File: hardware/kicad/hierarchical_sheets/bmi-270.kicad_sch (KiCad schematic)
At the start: 4 parts

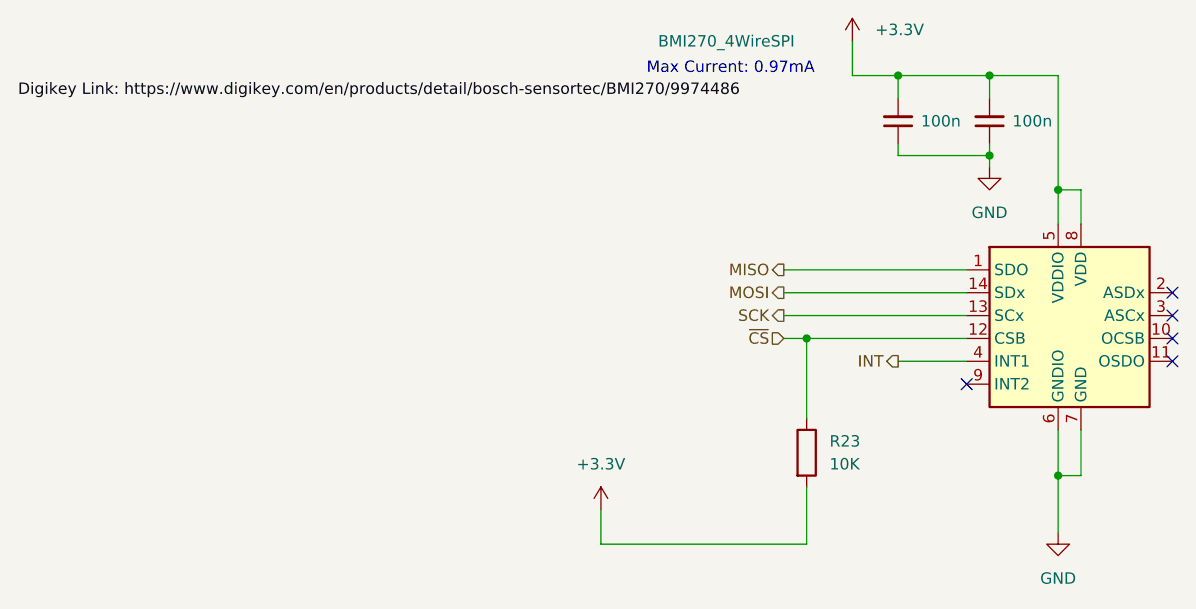
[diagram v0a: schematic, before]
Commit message: assigned footprints
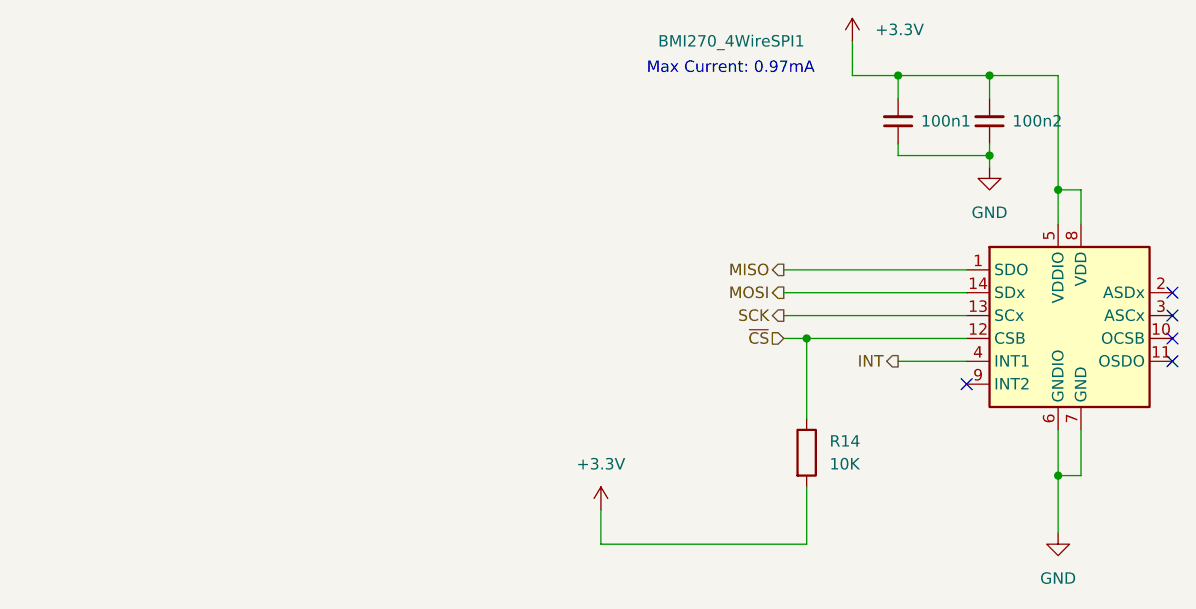
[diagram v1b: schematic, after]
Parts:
- 100n1, 100n2: renamed from 100n; footprint (none) -> Resistor_SMD:R_0603_1608Metric
- R14: renamed from R23; footprint (none) -> Resistor_SMD:R_0603_1608Metric
- renumbered BMI270_4WireSPI to BMI270_4WireSPI1
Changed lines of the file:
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@@
     (effects (font (size 1.27 1.27)) (justify left bottom))
   )
-  (label "Digikey Link: https:{slash}{slash}www.digikey.com{slash}en{slash}products{slash}detail{slash}bosch-sensortec{slash}BMI270{slash}9974486"
-    (at 13.97 77.47 0) (fields_autoplaced)
-    (effects (font (size 1.27 1.27)) (justify left bottom))
-  )
   (hierarchical_label "INT" (shape output) (at 111.76 106.68 180) (fields_autoplaced)
     (effects (font (size 1.27 1.27)) (justify right))
@@
   (symbol (lib_name "C_Small_1") (lib_id "Device:C_Small") (at 111.76 80.01 180) (unit 1)
     (in_bom yes) (on_board yes) (dnp no) (fields_autoplaced)
-    (property "Reference" "100n" (at 114.3 80.0036 0)
+    (property "Reference" "100n1" (at 114.3 80.0036 0)
       (effects (font (size 1.27 1.27)) (justify right))
     )
@@
       (effects (font (size 1.27 1.27)) (justify left) hide)
     )
-    (property "Footprint" "" (at 111.76 80.01 0)
+    (property "Footprint" "Resistor_SMD:R_0603_1608Metric" (at 111.76 80.01 0)
       (effects (font (size 1.27 1.27)) hide)
     )
@@
       (project "FC"
         (path "/54cce219-8b98-4e71-96c4-f9ee784aa3bc/7e43dc21-d4ed-4dfe-b96f-060fb7f0f8ce"
-          (reference "100n") (unit 1)
+          (reference "100n1") (unit 1)
         )
       )
@@
   (symbol (lib_id "BMI270:BMI270") (at 132.08 101.6 0) (unit 1)
     (in_bom yes) (on_board yes) (dnp no)
-    (property "Reference" "BMI270_4WireSPI" (at 85.09 71.12 0)
+    (property "Reference" "BMI270_4WireSPI1" (at 85.09 71.12 0)
       (effects (font (size 1.27 1.27)) (justify left))
     )
@@
       (project "FC"
         (path "/54cce219-8b98-4e71-96c4-f9ee784aa3bc/7e43dc21-d4ed-4dfe-b96f-060fb7f0f8ce"
-          (reference "BMI270_4WireSPI") (unit 1)
+          (reference "BMI270_4WireSPI1") (unit 1)
         )
       )
@@
   (symbol (lib_name "C_Small_1") (lib_id "Device:C_Small") (at 121.92 80.01 180) (unit 1)
     (in_bom yes) (on_board yes) (dnp no) (fields_autoplaced)
-    (property "Reference" "100n" (at 124.46 80.0036 0)
+    (property "Reference" "100n2" (at 124.46 80.0036 0)
       (effects (font (size 1.27 1.27)) (justify right))
     )
@@
       (effects (font (size 1.27 1.27)) (justify left) hide)
     )
-    (property "Footprint" "" (at 121.92 80.01 0)
+    (property "Footprint" "Resistor_SMD:R_0603_1608Metric" (at 121.92 80.01 0)
       (effects (font (size 1.27 1.27)) hide)
     )
@@
       (project "FC"
         (path "/54cce219-8b98-4e71-96c4-f9ee784aa3bc/7e43dc21-d4ed-4dfe-b96f-060fb7f0f8ce"
-          (reference "100n") (unit 1)
+          (reference "100n2") (unit 1)
         )
       )
@@
   (symbol (lib_id "power:+3.3V") (at 106.68 71.12 0) (unit 1)
     (in_bom yes) (on_board yes) (dnp no) (fields_autoplaced)
-    (property "Reference" "#PWR040" (at 106.68 74.93 0)
+    (property "Reference" "#PWR018" (at 106.68 74.93 0)
       (effects (font (size 1.27 1.27)) hide)
     )
@@
       (project "FC"
         (path "/54cce219-8b98-4e71-96c4-f9ee784aa3bc/7e43dc21-d4ed-4dfe-b96f-060fb7f0f8ce"
-          (reference "#PWR040") (unit 1)
+          (reference "#PWR018") (unit 1)
         )
       )
@@
   (symbol (lib_id "power:GND") (at 121.92 85.09 0) (unit 1)
     (in_bom yes) (on_board yes) (dnp no) (fields_autoplaced)
-    (property "Reference" "#PWR038" (at 121.92 91.44 0)
+    (property "Reference" "#PWR019" (at 121.92 91.44 0)
       (effects (font (size 1.27 1.27)) hide)
     )
@@
       (project "FC"
         (path "/54cce219-8b98-4e71-96c4-f9ee784aa3bc/7e43dc21-d4ed-4dfe-b96f-060fb7f0f8ce"
-          (reference "#PWR038") (unit 1)
+          (reference "#PWR019") (unit 1)
         )
       )
@@
   (symbol (lib_id "power:+3.3V") (at 78.74 123.19 0) (unit 1)
     (in_bom yes) (on_board yes) (dnp no) (fields_autoplaced)
-    (property "Reference" "#PWR041" (at 78.74 127 0)
+    (property "Reference" "#PWR017" (at 78.74 127 0)
       (effects (font (size 1.27 1.27)) hide)
     )
@@
       (project "FC"
         (path "/54cce219-8b98-4e71-96c4-f9ee784aa3bc/7e43dc21-d4ed-4dfe-b96f-060fb7f0f8ce"
-          (reference "#PWR041") (unit 1)
+          (reference "#PWR017") (unit 1)
         )
       )
@@
   (symbol (lib_id "power:GND") (at 129.54 125.73 0) (unit 1)
     (in_bom yes) (on_board yes) (dnp no) (fields_autoplaced)
-    (property "Reference" "#PWR037" (at 129.54 132.08 0)
+    (property "Reference" "#PWR020" (at 129.54 132.08 0)
       (effects (font (size 1.27 1.27)) hide)
     )
@@
       (project "FC"
         (path "/54cce219-8b98-4e71-96c4-f9ee784aa3bc/7e43dc21-d4ed-4dfe-b96f-060fb7f0f8ce"
-          (reference "#PWR037") (unit 1)
+          (reference "#PWR020") (unit 1)
         )
       )
@@
   (symbol (lib_id "Device:R") (at 101.6 116.84 0) (unit 1)
     (in_bom yes) (on_board yes) (dnp no) (fields_autoplaced)
-    (property "Reference" "R23" (at 104.14 115.57 0)
+    (property "Reference" "R14" (at 104.14 115.57 0)
       (effects (font (size 1.27 1.27)) (justify left))
     )
@@
       (effects (font (size 1.27 1.27)) (justify left))
     )
-    (property "Footprint" "" (at 99.822 116.84 90)
+    (property "Footprint" "Resistor_SMD:R_0603_1608Metric" (at 99.822 116.84 90)
       (effects (font (size 1.27 1.27)) hide)
     )
@@
       (project "FC"
         (path "/54cce219-8b98-4e71-96c4-f9ee784aa3bc/7e43dc21-d4ed-4dfe-b96f-060fb7f0f8ce"
-          (reference "R23") (unit 1)
-        )
-      )
+          (reference "R14") (unit 1)
+        )
+      )

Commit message: making formatting more consistent
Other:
- moved on the sheet: 100n1, 100n2, BMI270_4WireSPI1, R14

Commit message: formatting
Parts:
- renumbered BMI270_4WireSPI1 to U5
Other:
- title: SRAD-FC -> IMU (BMI-270)
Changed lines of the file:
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@@
   (paper "USLetter")
   (title_block
-    (title "SRAD-FC")
+    (title "IMU (BMI-270)")
     (company "Missouri S&T Rocket Design Team")
     (comment 1 "Evan Richard")
@@
   (symbol (lib_id "BMI270:BMI270") (at 154.94 97.155 0) (unit 1)
     (in_bom yes) (on_board yes) (dnp no)
-    (property "Reference" "BMI270_4WireSPI1" (at 107.95 66.675 0)
+    (property "Reference" "U5" (at 158.75 84.455 0)
       (effects (font (size 1.27 1.27)) (justify left))
     )
     (property "Value" "BMI270" (at 157.1341 86.995 0)
-      (effects (font (size 1.27 1.27)) (justify left) hide)
+      (effects (font (size 1.27 1.27)) (justify left))
     )
     (property "Footprint" "BMI270:XDCR_BMI270" (at 154.94 97.155 0)
@@
       (project "FC"
         (path "/54cce219-8b98-4e71-96c4-f9ee784aa3bc/7e43dc21-d4ed-4dfe-b96f-060fb7f0f8ce"
-          (reference "BMI270_4WireSPI1") (unit 1)
+          (reference "U5") (unit 1)
         )
       )

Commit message: sync
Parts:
- renumbered 100n1 to C28, 100n2 to C29
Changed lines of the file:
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@@
   (symbol (lib_name "C_Small_1") (lib_id "Device:C_Small") (at 134.62 75.565 180) (unit 1)
     (in_bom yes) (on_board yes) (dnp no) (fields_autoplaced)
-    (property "Reference" "100n1" (at 137.16 75.5586 0)
+    (property "Reference" "C28" (at 137.16 76.1936 0)
       (effects (font (size 1.27 1.27)) (justify right))
     )
@@
       (project "FC"
         (path "/54cce219-8b98-4e71-96c4-f9ee784aa3bc/7e43dc21-d4ed-4dfe-b96f-060fb7f0f8ce"
-          (reference "100n1") (unit 1)
+          (reference "C28") (unit 1)
         )
       )
@@
   (symbol (lib_name "C_Small_1") (lib_id "Device:C_Small") (at 144.78 75.565 180) (unit 1)
     (in_bom yes) (on_board yes) (dnp no) (fields_autoplaced)
-    (property "Reference" "100n2" (at 147.32 75.5586 0)
+    (property "Reference" "C29" (at 147.32 76.1936 0)
       (effects (font (size 1.27 1.27)) (justify right))
     )
@@
       (project "FC"
         (path "/54cce219-8b98-4e71-96c4-f9ee784aa3bc/7e43dc21-d4ed-4dfe-b96f-060fb7f0f8ce"
-          (reference "100n2") (unit 1)
+          (reference "C29") (unit 1)
         )
       )
